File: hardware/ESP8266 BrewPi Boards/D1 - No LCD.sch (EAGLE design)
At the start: 8 parts, among them J1 RJ11-4L-B

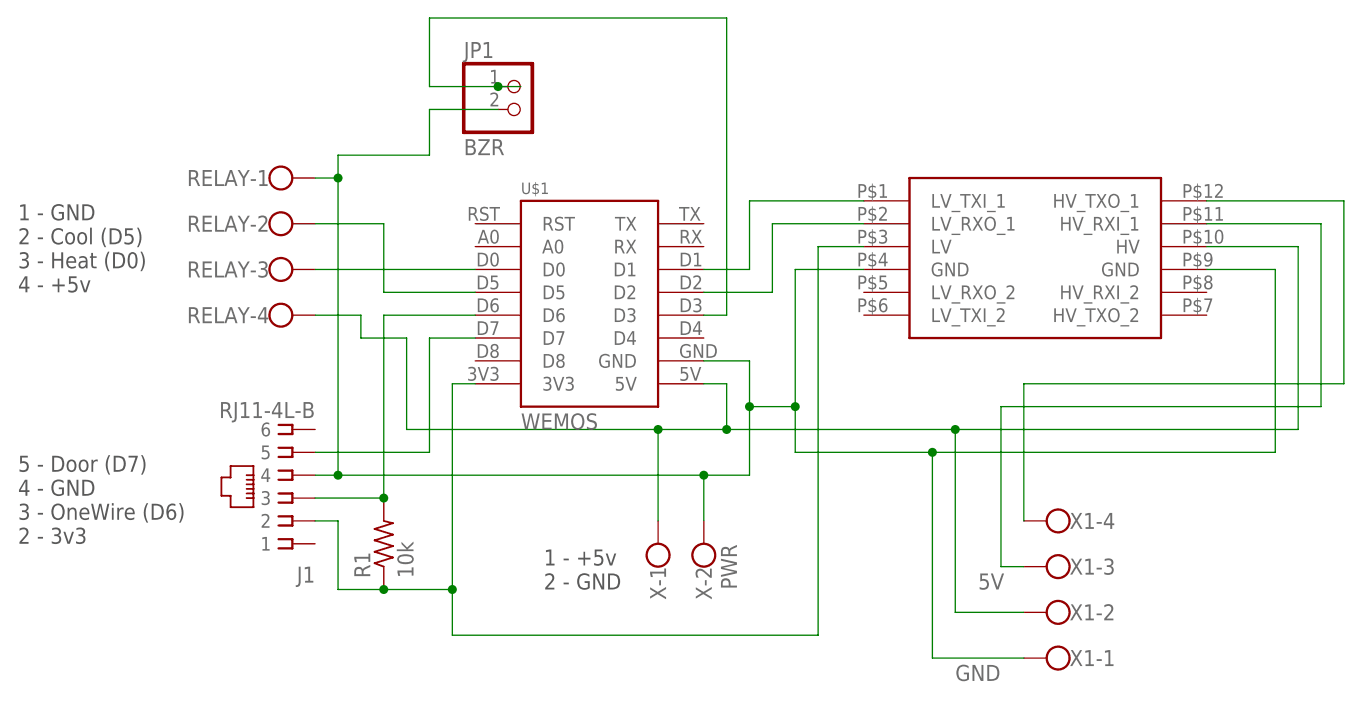
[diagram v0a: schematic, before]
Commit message: Updating docs & adding new eagle schematics
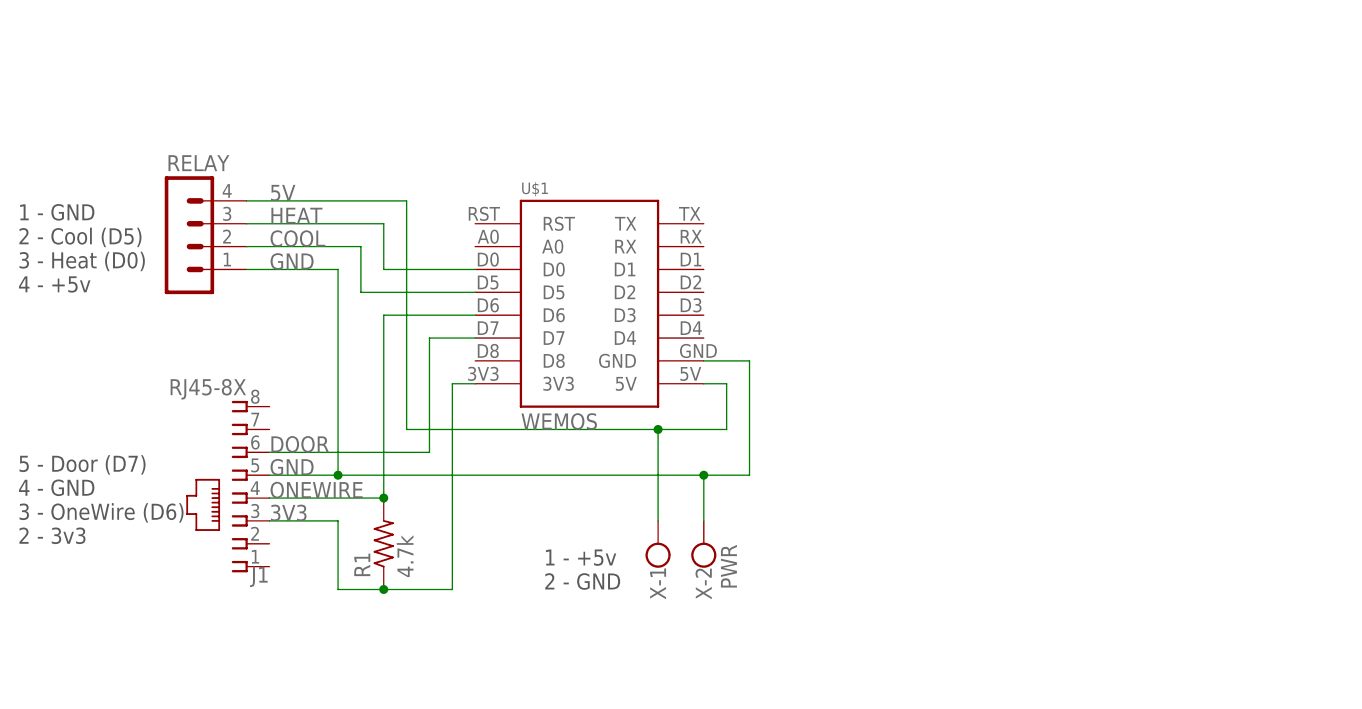
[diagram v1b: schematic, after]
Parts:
- removed JP1: BZR, pinhead:PINHD-1X2
- removed U$3: LOGIC_LEVEL_CONVERTER, SparkFun-Boards:LOGIC_LEVEL_CONVERTER
- removed X1: (no value), con-wago-500:W237-4
- J1: value RJ11-4L-B -> RJ45-8X; device con-tycoelectronics:RJ11-4L-B -> con-tycoelectronics:RJ45-8X
- R1: value 10k -> 4.7k; device rcl:R-US_0207/5V -> rcl:R-US_0309/12
- RELAY: device con-wago-500:W237-4 -> con-lstb:MA04-1
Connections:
- removed net D0: RELAY-3.KL, U$1.D0
- removed net D5: RELAY-2.KL, U$1.D5
- removed net D6: J1.3, R1.2, U$1.D6
- removed net D7: J1.5, U$1.D7
- removed net N$1: U$1.D1, U$3.LV_TXI_1
- removed net N$2: U$1.D2, U$3.LV_RXO_1
- removed net N$3: J1.2, R1.1, U$1.3V3, U$3.LV
- removed net N$4: U$3.HV_TXO_1, X1-4.KL
- removed net N$5: U$3.HV_RXI_1, X1-3.KL
- removed net N$6: JP1.1, U$1.D3
- new net 3V3: J1.3, R1.1, U$1.3V3
- new net COOL: RELAY.2, U$1.D5
- new net DOOR: J1.6, U$1.D7
- new net HEAT: RELAY.3, U$1.D0
- new net ONEWIRE: J1.4, R1.2, U$1.D6
- net 5V: now also RELAY.4; no longer RELAY-4.KL, U$3.HV, X1-2.KL
- net GND: now also J1.5, RELAY.1; no longer J1.4, JP1.2, RELAY-1.KL, U$3.GND, U$3.GND@2, X1-1.KL
